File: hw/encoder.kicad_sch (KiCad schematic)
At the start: 1 part, among them U5 LM2901

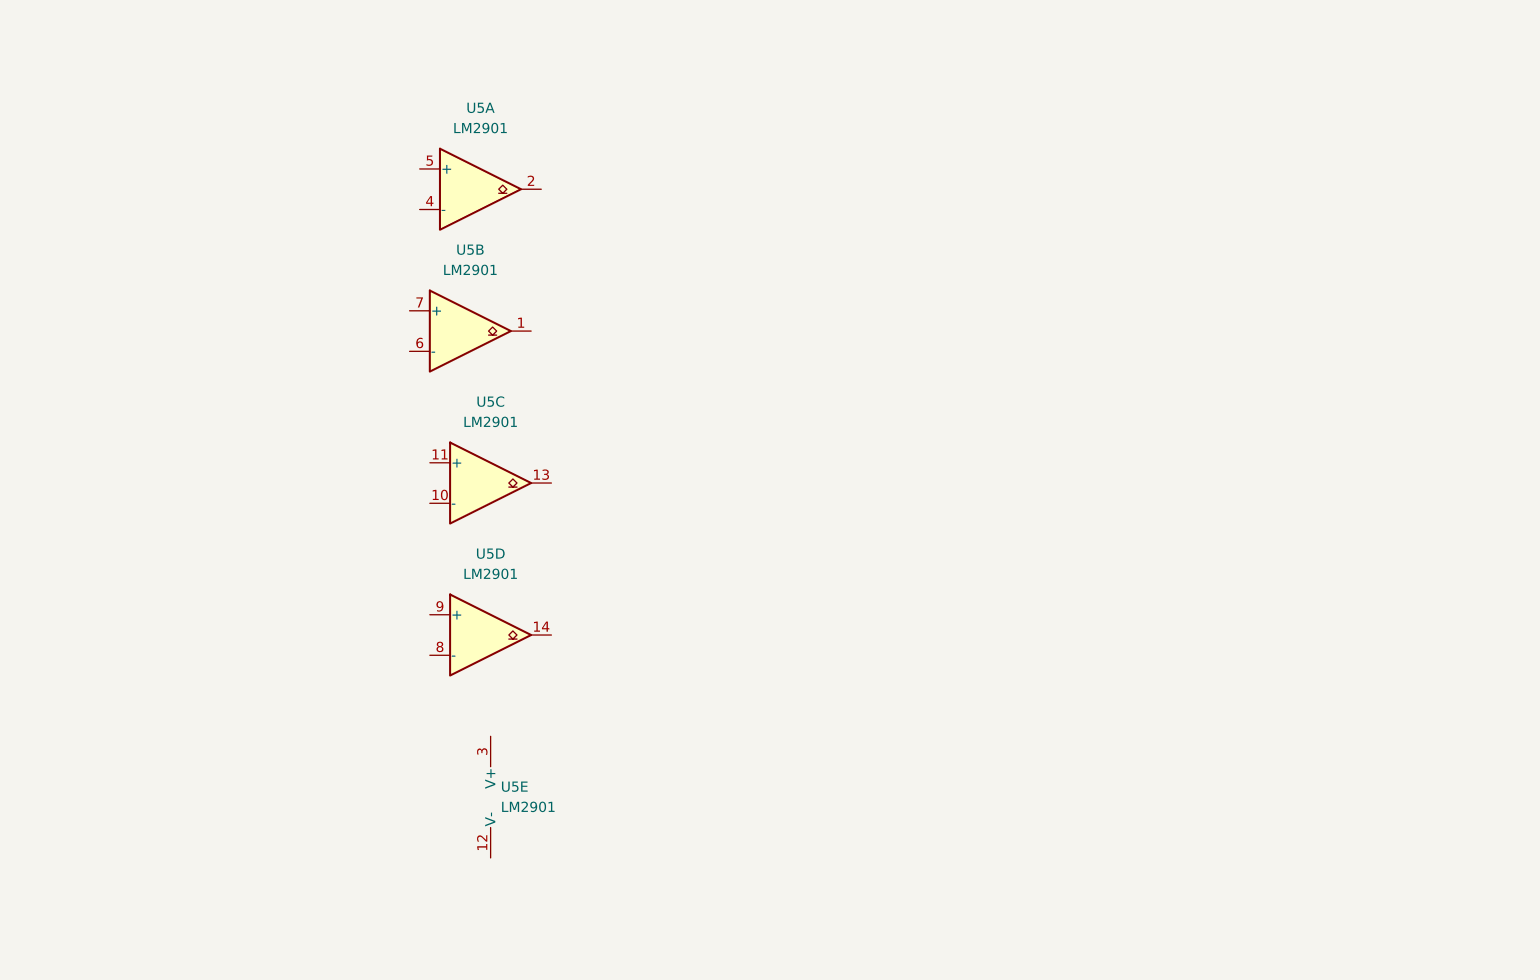
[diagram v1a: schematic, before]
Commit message: Update encoder circuit
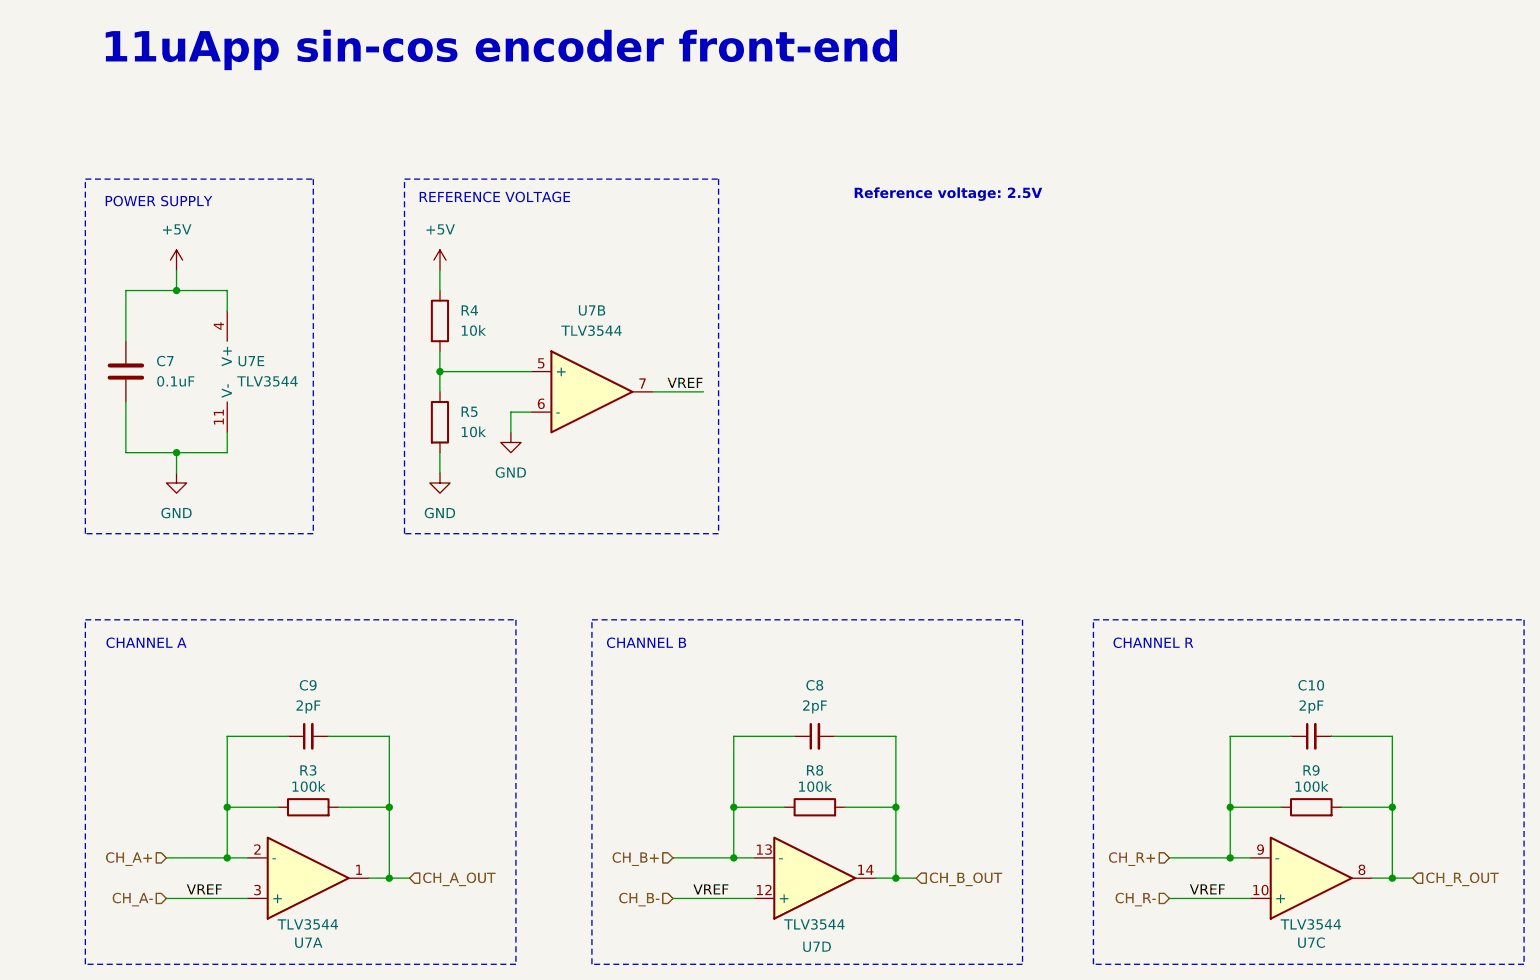
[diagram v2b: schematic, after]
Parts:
- removed U5: LM2901, symbol Comparator:LM2901
- added C10, C8, C9: 2pF, symbol Device:C_Small
- added C7: 0.1uF, symbol Device:C
- added R3, R8, R9: 100k, symbol Device:R
- added R4, R5: 10k, symbol Device:R
- added U7: TLV3544, symbol Device:Opamp_Quad
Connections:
- new net: R4.2, R5.1, U7.5 (+)
- new net +5V: C7.2, R4.1, U7.4 (V+)
- new net CH_A+: C9.1, R3.1, U7.2 (-)
- new net CH_A-: U7.10 (+), U7.12 (+), U7.3 (+), U7.7
- new net CH_A_OUT: C9.2, R3.2, U7.1
- new net CH_B+: C8.1, R8.1, U7.13 (-)
- new net CH_B_OUT: C8.2, R8.2, U7.14
- new net CH_R+: C10.1, R9.1, U7.9 (-)
- new net CH_R_OUT: C10.2, R9.2, U7.8
- new net GND: C7.1, R5.2, U7.11 (V-), U7.6 (-)
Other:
- note added: "11uApp sin-cos encoder front-end"
- note added: "CHANNEL A"
- note added: "CHANNEL B"
- note added: "CHANNEL R"
- note added: "POWER SUPPLY"
- note added: "REFERENCE VOLTAGE"
